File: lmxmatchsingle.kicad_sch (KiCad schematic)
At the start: 9 parts

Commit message: For Darrel
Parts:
- renumbered C228 to C182, C229 to C183, C230 to C184, L11 to L7, R94 to R199, R95 to R200, R228 to R201, R229 to R202, TP9 to TP10

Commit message: Add Clock sources and monitor output
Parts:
- renumbered C182 to C172, C183 to C173, C184 to C174, L7 to L6, R199 to R170, R200 to R171, R201 to R172, R202 to R173, TP10 to TP12

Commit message: Round 1 review comments
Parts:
- renumbered C172 to C189, C173 to C190, C174 to C191, R170 to R210, R171 to R211, R172 to R212, R173 to R213

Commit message: Round 2 Review, power tree cleanup
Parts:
- renumbered C189 to C191, C190 to C192, C191 to C193, R210 to R222, R211 to R223, R212 to R224, R213 to R225

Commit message: Darrel Suggestions
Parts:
- removed TP12: TPLO, Connector_Coaxial:CoaxialSwitch_Hirose_MS-156C3_Horizontal, symbol Connector:CoaxialSwitch_Testpoint
- renumbered C191 to C192, C192 to C193, C193 to C194, L6 to L4
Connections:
- net OUT: now also C193.2
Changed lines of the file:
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@@
-	(wire
-		(pts
-			(xy 157.48 77.47) (xy 161.29 77.47)
-		)
-		(stroke
-			(width 0)
-			(type default)
-		)
-	)
 	(wire
 		(pts
@@
 	(wire
 		(pts
-			(xy 161.29 80.01) (xy 161.29 97.79)
-		)
-		(stroke
-			(width 0)
-			(type default)
-		)
-	)
-	(wire
-		(pts
 			(xy 115.57 95.25) (xy 118.11 95.25)
 		)
@@
 		(pts
 			(xy 118.11 77.47) (xy 129.54 77.47)
-		)
-		(stroke
-			(width 0)
-			(type default)
-		)
-	)
-	(wire
-		(pts
-			(xy 161.29 80.01) (xy 157.48 80.01)
 		)
 		(stroke
@@
 	(hierarchical_label "OUT"
 		(shape input)
-		(at 161.29 77.47 0)
+		(at 147.32 77.47 0)
 		(effects
 			(font
@@
 		(in_pos_files yes)
 		(dnp no)
-		(property "Reference" "C191"
+		(property "Reference" "C192"
 			(at 123.19 100.584 90)
 			(show_name no)
@@
 			(project "huskypointofload"
 				(path "/eb9c972b-d134-41da-be97-ece3f463f7e0/999a5927-21bb-4ea7-ad27-c6446933693a/87e75886-8a53-478a-8ff0-cf0e99af78d2"
-					(reference "C191")
+					(reference "C192")
 					(unit 1)
 				)
 				(path "/eb9c972b-d134-41da-be97-ece3f463f7e0/999a5927-21bb-4ea7-ad27-c6446933693a/e51e609f-c5bf-403c-8ca6-81342f1b9050"
-					(reference "C229")
+					(reference "C230")
 					(unit 1)
 				)
 				(path "/eb9c972b-d134-41da-be97-ece3f463f7e0/999a5927-21bb-4ea7-ad27-c6446933693a/f37470a5-aa7e-4685-99e3-8b4186c25acc"
-					(reference "C232")
+					(reference "C233")
 					(unit 1)
 				)
@@
 		(in_pos_files yes)
 		(dnp no)
-		(property "Reference" "C192"
+		(property "Reference" "C193"
 			(at 132.08 82.804 90)
 			(show_name no)
@@
 			(project "huskypointofload"
 				(path "/eb9c972b-d134-41da-be97-ece3f463f7e0/999a5927-21bb-4ea7-ad27-c6446933693a/87e75886-8a53-478a-8ff0-cf0e99af78d2"
-					(reference "C192")
+					(reference "C193")
 					(unit 1)
 				)
 				(path "/eb9c972b-d134-41da-be97-ece3f463f7e0/999a5927-21bb-4ea7-ad27-c6446933693a/e51e609f-c5bf-403c-8ca6-81342f1b9050"
-					(reference "C230")
+					(reference "C231")
 					(unit 1)
 				)
 				(path "/eb9c972b-d134-41da-be97-ece3f463f7e0/999a5927-21bb-4ea7-ad27-c6446933693a/f37470a5-aa7e-4685-99e3-8b4186c25acc"
-					(reference "C233")
-					(unit 1)
-				)
-			)
-		)
-	)
-	(symbol
-		(lib_id "power:GND")
-		(at 161.29 97.79 0)
-		(unit 1)
-		(body_style 1)
-		(exclude_from_sim no)
-		(in_bom yes)
-		(on_board yes)
-		(in_pos_files yes)
-		(dnp no)
-		(fields_autoplaced yes)
-		(property "Reference" "#PWR0246"
-			(at 161.29 104.14 0)
-			(hide yes)
-			(show_name no)
-			(do_not_autoplace no)
-			(effects
-				(font
-					(size 1.27 1.27)
-				)
-			)
-		)
-		(property "Value" "GND"
-			(at 161.29 102.87 0)
-			(show_name no)
-			(do_not_autoplace no)
-			(effects
-				(font
-					(size 1.27 1.27)
-				)
-			)
-		)
-		(property "Footprint" ""
-			(at 161.29 97.79 0)
-			(hide yes)
-			(show_name no)
-			(do_not_autoplace no)
-			(effects
-				(font
-					(size 1.27 1.27)
-				)
-			)
-		)
-		(property "Datasheet" ""
-			(at 161.29 97.79 0)
-			(hide yes)
-			(show_name no)
-			(do_not_autoplace no)
-			(effects
-				(font
-					(size 1.27 1.27)
-				)
-			)
-		)
-		(property "Description" "Power symbol creates a global label with name \"GND\" , ground"
-			(at 161.29 97.79 0)
-			(hide yes)
-			(show_name no)
-			(do_not_autoplace no)
-			(effects
-				(font
-					(size 1.27 1.27)
-				)
-			)
-		)
-		(pin "1"
-		)
-		(instances
-			(project "huskypointofload"
-				(path "/eb9c972b-d134-41da-be97-ece3f463f7e0/999a5927-21bb-4ea7-ad27-c6446933693a/87e75886-8a53-478a-8ff0-cf0e99af78d2"
-					(reference "#PWR0246")
-					(unit 1)
-				)
-				(path "/eb9c972b-d134-41da-be97-ece3f463f7e0/999a5927-21bb-4ea7-ad27-c6446933693a/e51e609f-c5bf-403c-8ca6-81342f1b9050"
-					(reference "#PWR0270")
-					(unit 1)
-				)
-				(path "/eb9c972b-d134-41da-be97-ece3f463f7e0/999a5927-21bb-4ea7-ad27-c6446933693a/f37470a5-aa7e-4685-99e3-8b4186c25acc"
-					(reference "#PWR0274")
+					(reference "C234")
 					(unit 1)
 				)
@@
 		(dnp no)
 		(fields_autoplaced yes)
-		(property "Reference" "#PWR0243"
+		(property "Reference" "#PWR0247"
 			(at 118.11 129.54 0)
 			(hide yes)
@@
 			(project "huskypointofload"
 				(path "/eb9c972b-d134-41da-be97-ece3f463f7e0/999a5927-21bb-4ea7-ad27-c6446933693a/87e75886-8a53-478a-8ff0-cf0e99af78d2"
-					(reference "#PWR0243")
+					(reference "#PWR0247")
 					(unit 1)
 				)
 				(path "/eb9c972b-d134-41da-be97-ece3f463f7e0/999a5927-21bb-4ea7-ad27-c6446933693a/e51e609f-c5bf-403c-8ca6-81342f1b9050"
-					(reference "#PWR0267")
+					(reference "#PWR0270")
 					(unit 1)
 				)
 				(path "/eb9c972b-d134-41da-be97-ece3f463f7e0/999a5927-21bb-4ea7-ad27-c6446933693a/f37470a5-aa7e-4685-99e3-8b4186c25acc"
-					(reference "#PWR0271")
+					(reference "#PWR0273")
 					(unit 1)
 				)
@@
 		(in_pos_files yes)
 		(dnp no)
-		(property "Reference" "C193"
+		(property "Reference" "C194"
 			(at 132.08 118.364 90)
 			(show_name no)
@@
 			(project "huskypointofload"
 				(path "/eb9c972b-d134-41da-be97-ece3f463f7e0/999a5927-21bb-4ea7-ad27-c6446933693a/87e75886-8a53-478a-8ff0-cf0e99af78d2"
-					(reference "C193")
+					(reference "C194")
 					(unit 1)
 				)
 				(path "/eb9c972b-d134-41da-be97-ece3f463f7e0/999a5927-21bb-4ea7-ad27-c6446933693a/e51e609f-c5bf-403c-8ca6-81342f1b9050"
-					(reference "C231")
+					(reference "C232")
 					(unit 1)
 				)
 				(path "/eb9c972b-d134-41da-be97-ece3f463f7e0/999a5927-21bb-4ea7-ad27-c6446933693a/f37470a5-aa7e-4685-99e3-8b4186c25acc"
-					(reference "C234")
+					(reference "C235")
 					(unit 1)
 				)
@@
 		(dnp no)
 		(fields_autoplaced yes)
-		(property "Reference" "#PWR0244"
+		(property "Reference" "#PWR0248"
 			(at 128.27 104.14 0)
 			(hide yes)
@@
 			(project "huskypointofload"
 				(path "/eb9c972b-d134-41da-be97-ece3f463f7e0/999a5927-21bb-4ea7-ad27-c6446933693a/87e75886-8a53-478a-8ff0-cf0e99af78d2"
-					(reference "#PWR0244")
+					(reference "#PWR0248")
 					(unit 1)
 				)
 				(path "/eb9c972b-d134-41da-be97-ece3f463f7e0/999a5927-21bb-4ea7-ad27-c6446933693a/e51e609f-c5bf-403c-8ca6-81342f1b9050"
-					(reference "#PWR0268")
+					(reference "#PWR0271")
 					(unit 1)
 				)
 				(path "/eb9c972b-d134-41da-be97-ece3f463f7e0/999a5927-21bb-4ea7-ad27-c6446933693a/f37470a5-aa7e-4685-99e3-8b4186c25acc"
-					(reference "#PWR0272")
+					(reference "#PWR0274")
 					(unit 1)
 				)
@@
 		(in_pos_files yes)
 		(dnp no)
-		(property "Reference" "L6"
+		(property "Reference" "L4"
 			(at 113.03 89.916 90)
 			(show_name no)
@@
 			(project "huskypointofload"
 				(path "/eb9c972b-d134-41da-be97-ece3f463f7e0/999a5927-21bb-4ea7-ad27-c6446933693a/87e75886-8a53-478a-8ff0-cf0e99af78d2"
+					(reference "L4")
+					(unit 1)
+				)
+				(path "/eb9c972b-d134-41da-be97-ece3f463f7e0/999a5927-21bb-4ea7-ad27-c6446933693a/e51e609f-c5bf-403c-8ca6-81342f1b9050"
 					(reference "L6")
 					(unit 1)
 				)
-				(path "/eb9c972b-d134-41da-be97-ece3f463f7e0/999a5927-21bb-4ea7-ad27-c6446933693a/e51e609f-c5bf-403c-8ca6-81342f1b9050"
-					(reference "L8")
-					(unit 1)
-				)
 				(path "/eb9c972b-d134-41da-be97-ece3f463f7e0/999a5927-21bb-4ea7-ad27-c6446933693a/f37470a5-aa7e-4685-99e3-8b4186c25acc"
-					(reference "L9")
+					(reference "L7")
 					(unit 1)
 				)
@@
 		(dnp no)
 		(fields_autoplaced yes)
-		(property "Reference" "#PWR0245"
+		(property "Reference" "#PWR0249"
 			(at 147.32 129.54 0)
 			(hide yes)
@@
 			(project "huskypointofload"
 				(path "/eb9c972b-d134-41da-be97-ece3f463f7e0/999a5927-21bb-4ea7-ad27-c6446933693a/87e75886-8a53-478a-8ff0-cf0e99af78d2"
-					(reference "#PWR0245")
+					(reference "#PWR0249")
 					(unit 1)
 				)
 				(path "/eb9c972b-d134-41da-be97-ece3f463f7e0/999a5927-21bb-4ea7-ad27-c6446933693a/e51e609f-c5bf-403c-8ca6-81342f1b9050"
-					(reference "#PWR0269")
+					(reference "#PWR0272")
 					(unit 1)
 				)
 				(path "/eb9c972b-d134-41da-be97-ece3f463f7e0/999a5927-21bb-4ea7-ad27-c6446933693a/f37470a5-aa7e-4685-99e3-8b4186c25acc"
-					(reference "#PWR0273")
-					(unit 1)
-				)
-			)
-		)
-	)
-	(symbol
-		(lib_id "Connector:CoaxialSwitch_Testpoint")
-		(at 152.4 78.74 0)
-		(unit 1)
-		(body_style 1)
-		(exclude_from_sim no)
-		(in_bom yes)
-		(on_board yes)
-		(in_pos_files yes)
-		(dnp no)
-		(property "Reference" "TP12"
-			(at 152.4 71.12 0)
-			(show_name no)
-			(do_not_autoplace no)
-			(effects
-				(font
-					(size 1.27 1.27)
-				)
-			)
-		)
-		(property "Value" "TPLO"
-			(at 152.4 73.66 0)
-			(show_name no)
-			(do_not_autoplace no)
-			(effects
-				(font
-					(size 1.27 1.27)
-				)
-			)
-		)
-		(property "Footprint" "Connector_Coaxial:CoaxialSwitch_Hirose_MS-156C3_Horizontal"
-			(at 152.4 77.47 0)
-			(hide yes)
-			(show_name no)
-			(do_not_autoplace no)
-			(effects
-				(font
-					(size 1.27 1.27)
-				)
-			)
-		)
-		(property "Datasheet" ""
-			(at 152.4 77.47 0)
-			(hide yes)
-			(show_name no)
-			(do_not_autoplace no)
-			(effects
-				(font
-					(size 1.27 1.27)
-				)
-			)
-		)
-		(property "Description" "Subminiature Coaxial Switch testpoint"
-			(at 152.4 78.74 0)
-			(hide yes)
-			(show_name no)
-			(do_not_autoplace no)
-			(effects
-				(font
-					(size 1.27 1.27)
-				)
-			)
-		)
-		(pin "C"
-		)
-		(pin "A"
-		)
-		(pin "G"
-		)
-		(instances
-			(project "huskypointofload"
-				(path "/eb9c972b-d134-41da-be97-ece3f463f7e0/999a5927-21bb-4ea7-ad27-c6446933693a/87e75886-8a53-478a-8ff0-cf0e99af78d2"
-					(reference "TP12")
-					(unit 1)
-				)
-				(path "/eb9c972b-d134-41da-be97-ece3f463f7e0/999a5927-21bb-4ea7-ad27-c6446933693a/e51e609f-c5bf-403c-8ca6-81342f1b9050"
-					(reference "TP13")
-					(unit 1)
-				)
-				(path "/eb9c972b-d134-41da-be97-ece3f463f7e0/999a5927-21bb-4ea7-ad27-c6446933693a/f37470a5-aa7e-4685-99e3-8b4186c25acc"
-					(reference "TP14")
-					(unit 1)
-				)
+					(reference "#PWR0275")
+					(unit 1)
+				)

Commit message: Passive footprint pass
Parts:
- C192, C193, C194: footprint (none) -> Capacitor_SMD:C_0402_1005Metric
- R222, R223, R224, R225: footprint (none) -> Resistor_SMD:R_0402_1005Metric
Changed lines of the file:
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@@
 			)
 		)
-		(property "Footprint" ""
+		(property "Footprint" "Resistor_SMD:R_0402_1005Metric"
 			(at 118.11 118.11 0)
 			(hide yes)
@@
 			)
 		)
-		(property "Footprint" ""
+		(property "Footprint" "Capacitor_SMD:C_0402_1005Metric"
 			(at 123.19 95.25 0)
 			(hide yes)
@@
 			)
 		)
-		(property "Footprint" ""
+		(property "Footprint" "Capacitor_SMD:C_0402_1005Metric"
 			(at 132.08 77.47 0)
 			(hide yes)
@@
 			)
 		)
-		(property "Footprint" ""
+		(property "Footprint" "Resistor_SMD:R_0402_1005Metric"
 			(at 118.11 82.55 0)
 			(hide yes)
@@
 			)
 		)
-		(property "Footprint" ""
+		(property "Footprint" "Resistor_SMD:R_0402_1005Metric"
 			(at 118.11 107.95 0)
 			(hide yes)
@@
 			)
 		)
-		(property "Footprint" ""
+		(property "Footprint" "Resistor_SMD:R_0402_1005Metric"
 			(at 147.32 118.11 0)
 			(hide yes)
@@
 			)
 		)
-		(property "Footprint" ""
+		(property "Footprint" "Capacitor_SMD:C_0402_1005Metric"
 			(at 132.08 113.03 0)
 			(hide yes)

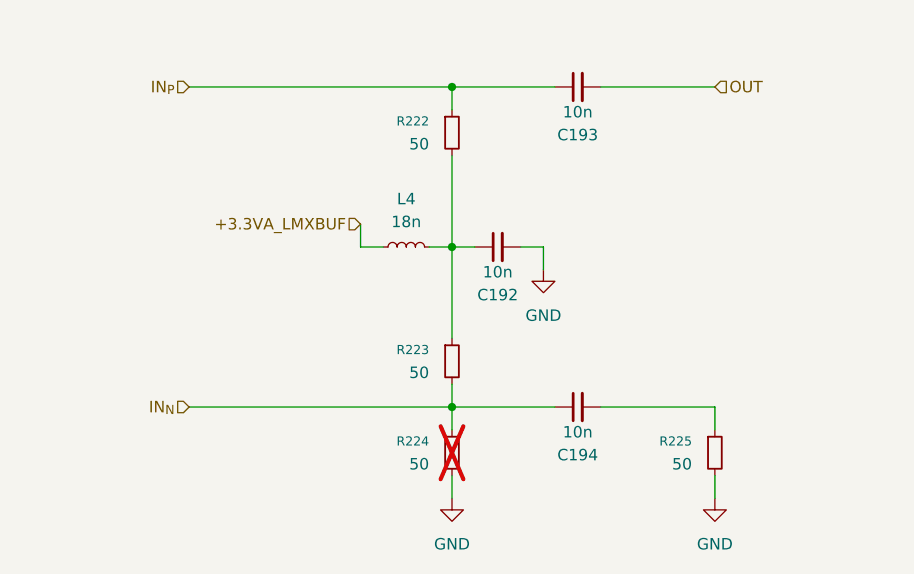
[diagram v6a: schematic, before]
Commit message: add NC and fix ERC
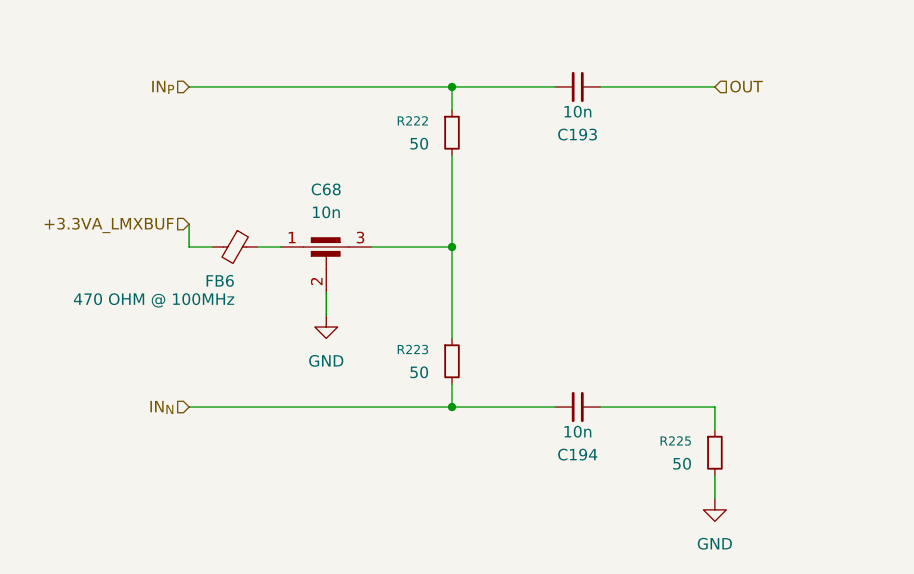
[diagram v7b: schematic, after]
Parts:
- removed C192: 10n, Capacitor_SMD:C_0402_1005Metric, symbol Device:C_Small
- removed L4: 18n, symbol Device:L_Small
- removed R224: 50, Resistor_SMD:R_0402_1005Metric, symbol Device:R_Small
- added C68: 10n, symbol Device:C_Feedthrough
- added FB6: 470 OHM @ 100MHz, Inductor_SMD:L_0402_1005Metric, symbol Device:FerriteBead_Small
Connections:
- net +3.3VA_LMXBUF: now also FB6.2
- net GND: now also C68.2
- net at R222.2, R223.1: now also C68.3
- new net: C68.1, FB6.1
